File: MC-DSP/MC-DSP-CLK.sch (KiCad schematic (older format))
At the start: 8 parts

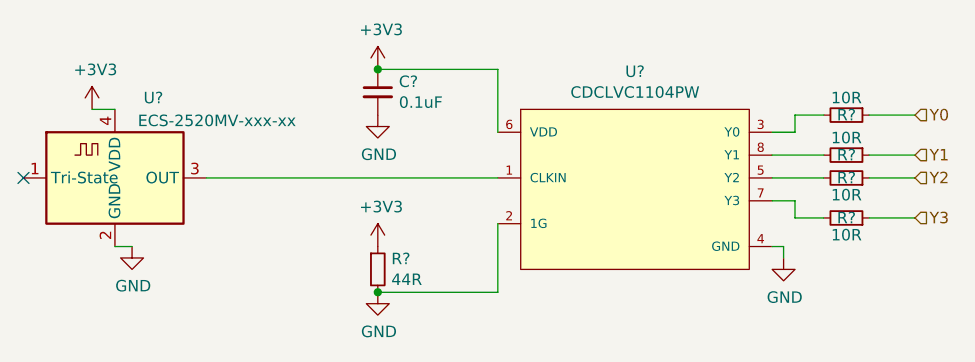
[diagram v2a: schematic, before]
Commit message: All parts labeled, just need to pick passives basically.
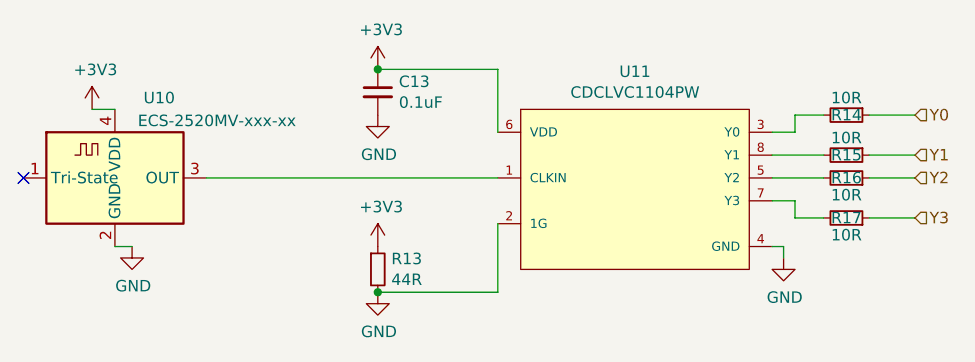
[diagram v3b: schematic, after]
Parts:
- C13: renamed from C?; footprint (none) -> Capacitor_SMD:C_0201_0603Metric_Pad0.64x0.40mm_HandSolder
- R13, R14, R15, R16, R17: renamed from R?; footprint (none) -> Resistor_SMD:R_0603_1608Metric_Pad0.98x0.95mm_HandSolder
- gave numbers to parts that had none: 2
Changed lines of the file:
@@
 $EndDescr
 $Comp
-L Oscillator:ECS-2520MV-xxx-xx U?
+L Oscillator:ECS-2520MV-xxx-xx U10
 U 1 1 61A52BCE
 P 5225 3750
-F 0 "U?" H 5350 4100 50  0000 L CNN
+F 0 "U10" H 5350 4100 50  0000 L CNN
 F 1 "ECS-2520MV-xxx-xx" H 5325 4000 50  0000 L CNN
 F 2 "Oscillator:Oscillator_SMD_ECS_2520MV-xxx-xx-4Pin_2.5x2.0mm" H 5675 3400 50  0001 C CNN
@@
 NoConn ~ 4825 3750
 $Comp
-L eec:CDCLVC1104PW U?
+L eec:CDCLVC1104PW U11
 U 1 1 61A56488
 P 6800 3550
-F 0 "U?" H 7500 3815 50  0000 C CNN
+F 0 "U11" H 7500 3815 50  0000 C CNN
 F 1 "CDCLVC1104PW" H 7500 3724 50  0000 C CNN
 F 2 "Texas_Instruments-PW0008A-0-0-*" H 6800 3950 50  0001 L CNN
@@
 	5625 3750 6900 3750
 $Comp
-L Device:C_Small C?
+L Device:C_Small C13
 U 1 1 61A5EB87
 P 6375 3375
-F 0 "C?" H 6467 3421 50  0000 L CNN
+F 0 "C13" H 6467 3421 50  0000 L CNN
 F 1 "0.1uF" H 6467 3330 50  0000 L CNN
-F 2 "" H 6375 3375 50  0001 C CNN
-F 3 "~" H 6375 3375 50  0001 C CNN
+F 2 "Capacitor_SMD:C_0201_0603Metric_Pad0.64x0.40mm_HandSolder" H 6375 3375 50  0001 C CNN
+F 3 "?" H 6375 3375 50  0001 C CNN
 	1    6375 3375
 	1    0    0    -1
@@
 Connection ~ 6375 4250
 $Comp
-L Device:R_Small R?
+L Device:R_Small R13
 U 1 1 61A628CF
 P 6375 4150
-F 0 "R?" H 6434 4196 50  0000 L CNN
+F 0 "R13" H 6434 4196 50  0000 L CNN
 F 1 "44R" H 6434 4105 50  0000 L CNN
-F 2 "" H 6375 4150 50  0001 C CNN
-F 3 "~" H 6375 4150 50  0001 C CNN
+F 2 "Resistor_SMD:R_0603_1608Metric_Pad0.98x0.95mm_HandSolder" H 6375 4150 50  0001 C CNN
+F 3 "?" H 6375 4150 50  0001 C CNN
 	1    6375 4150
 	1    0    0    -1
@@
 	8150 4050 8100 4050
 $Comp
-L Device:R_Small R?
+L Device:R_Small R14
 U 1 1 61A64470
 P 8425 3475
-F 0 "R?" V 8425 3475 50  0000 C CNN
+F 0 "R14" V 8425 3475 50  0000 C CNN
 F 1 "10R" V 8350 3475 50  0000 C CNN
-F 2 "" H 8425 3475 50  0001 C CNN
-F 3 "~" H 8425 3475 50  0001 C CNN
+F 2 "Resistor_SMD:R_0603_1608Metric_Pad0.98x0.95mm_HandSolder" H 8425 3475 50  0001 C CNN
+F 3 "?" H 8425 3475 50  0001 C CNN
 	1    8425 3475
 	0    1    1    0
 $EndComp
 $Comp
-L Device:R_Small R?
+L Device:R_Small R15
 U 1 1 61A6549D
 P 8425 3650
-F 0 "R?" V 8425 3650 50  0000 C CNN
+F 0 "R15" V 8425 3650 50  0000 C CNN
 F 1 "10R" V 8350 3650 50  0000 C CNN
-F 2 "" H 8425 3650 50  0001 C CNN
-F 3 "~" H 8425 3650 50  0001 C CNN
+F 2 "Resistor_SMD:R_0603_1608Metric_Pad0.98x0.95mm_HandSolder" H 8425 3650 50  0001 C CNN
+F 3 "?" H 8425 3650 50  0001 C CNN
 	1    8425 3650
 	0    1    1    0
 $EndComp
 $Comp
-L Device:R_Small R?
+L Device:R_Small R16
 U 1 1 61A657A3
 P 8425 3750
-F 0 "R?" V 8425 3750 50  0000 C CNN
+F 0 "R16" V 8425 3750 50  0000 C CNN
 F 1 "10R" V 8350 3750 50  0000 C CNN
-F 2 "" H 8425 3750 50  0001 C CNN
-F 3 "~" H 8425 3750 50  0001 C CNN
+F 2 "Resistor_SMD:R_0603_1608Metric_Pad0.98x0.95mm_HandSolder" H 8425 3750 50  0001 C CNN
+F 3 "?" H 8425 3750 50  0001 C CNN
 	1    8425 3750
 	0    1    -1   0
 $EndComp
 $Comp
-L Device:R_Small R?
+L Device:R_Small R17
 U 1 1 61A65A07
 P 8425 3925
-F 0 "R?" V 8425 3925 50  0000 C CNN
+F 0 "R17" V 8425 3925 50  0000 C CNN
 F 1 "10R" V 8350 3925 50  0000 C CNN
-F 2 "" H 8425 3925 50  0001 C CNN
-F 3 "~" H 8425 3925 50  0001 C CNN
+F 2 "Resistor_SMD:R_0603_1608Metric_Pad0.98x0.95mm_HandSolder" H 8425 3925 50  0001 C CNN
+F 3 "?" H 8425 3925 50  0001 C CNN
 	1    8425 3925
 	0    1    -1   0

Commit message: Removed clock buffer, misc leds, ethernet
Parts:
- C13: footprint Capacitor_SMD:C_0201_0603Metric_Pad0.64x0.40mm_HandSolder -> Capacitor_SMD:C_0603_1608Metric_Pad1.08x0.95mm_HandSolder
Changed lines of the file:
@@
 $Descr A4 11693 8268
 encoding utf-8
-Sheet 4 9
+Sheet 4 8
 Title ""
 Date ""
@@
 F 0 "C13" H 6467 3421 50  0000 L CNN
 F 1 "0.1uF" H 6467 3330 50  0000 L CNN
-F 2 "Capacitor_SMD:C_0201_0603Metric_Pad0.64x0.40mm_HandSolder" H 6375 3375 50  0001 C CNN
+F 2 "Capacitor_SMD:C_0603_1608Metric_Pad1.08x0.95mm_HandSolder" H 6375 3375 50  0001 C CNN
 F 3 "https://www.digikey.com/en/products/detail/yageo/CC0603KRX7R9BB104/2103082" H 6375 3375 50  0001 C CNN
 	1    6375 3375
